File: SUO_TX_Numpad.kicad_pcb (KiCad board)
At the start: 2 copper layers, 79.1 x 127.6 mm, 93 parts, among them J1 USB_C_Receptacle_USB2.0_16P, SW1 BOOT, U1 STM32F411CEUx, U2 XC6206PxxxMR-Regulator_Linear, U3 USBLC6-2SC6

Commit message: Added LCSC, but going to switch to 0603 or 0804 components as I want to keep handsoldering an option
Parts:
- F1: value Fuse 1500mA Fast -> Fuse 1A Fast

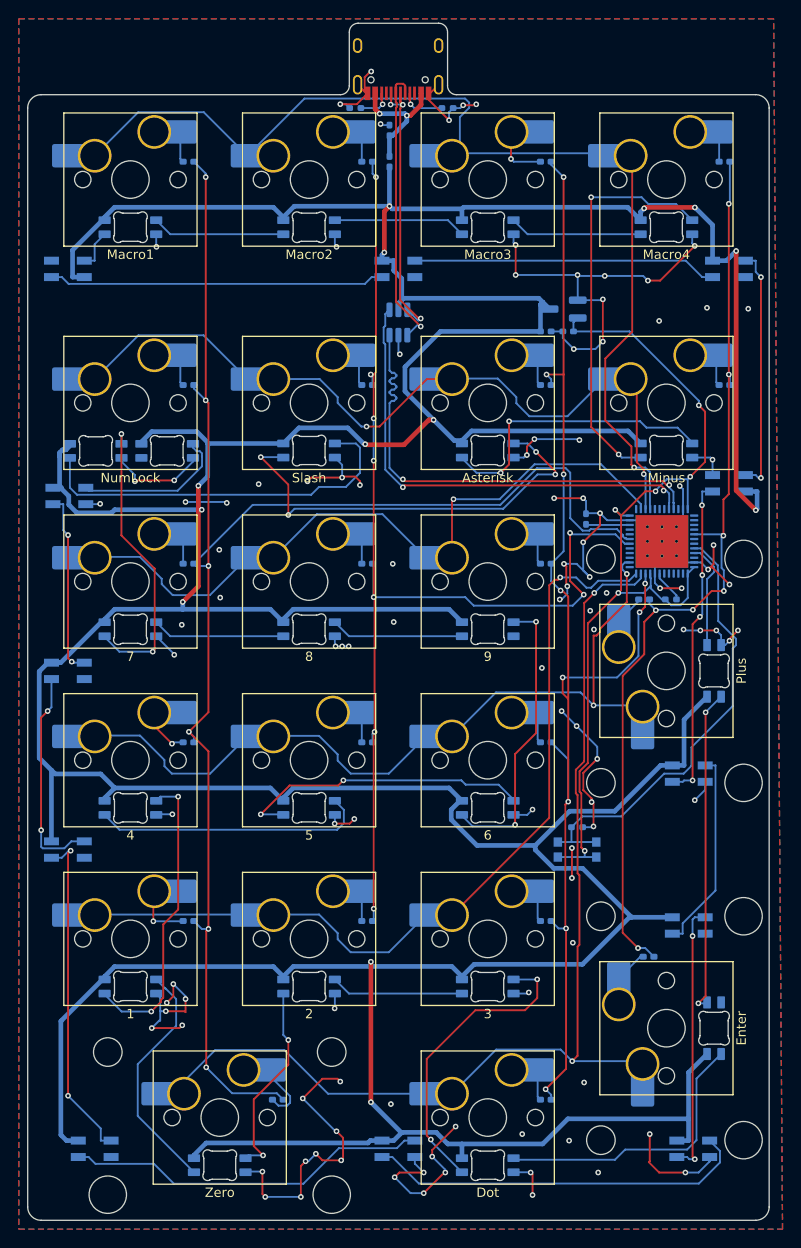
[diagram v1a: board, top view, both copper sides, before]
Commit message: Switched to 0805 for R C and SOD-123 for Diodes
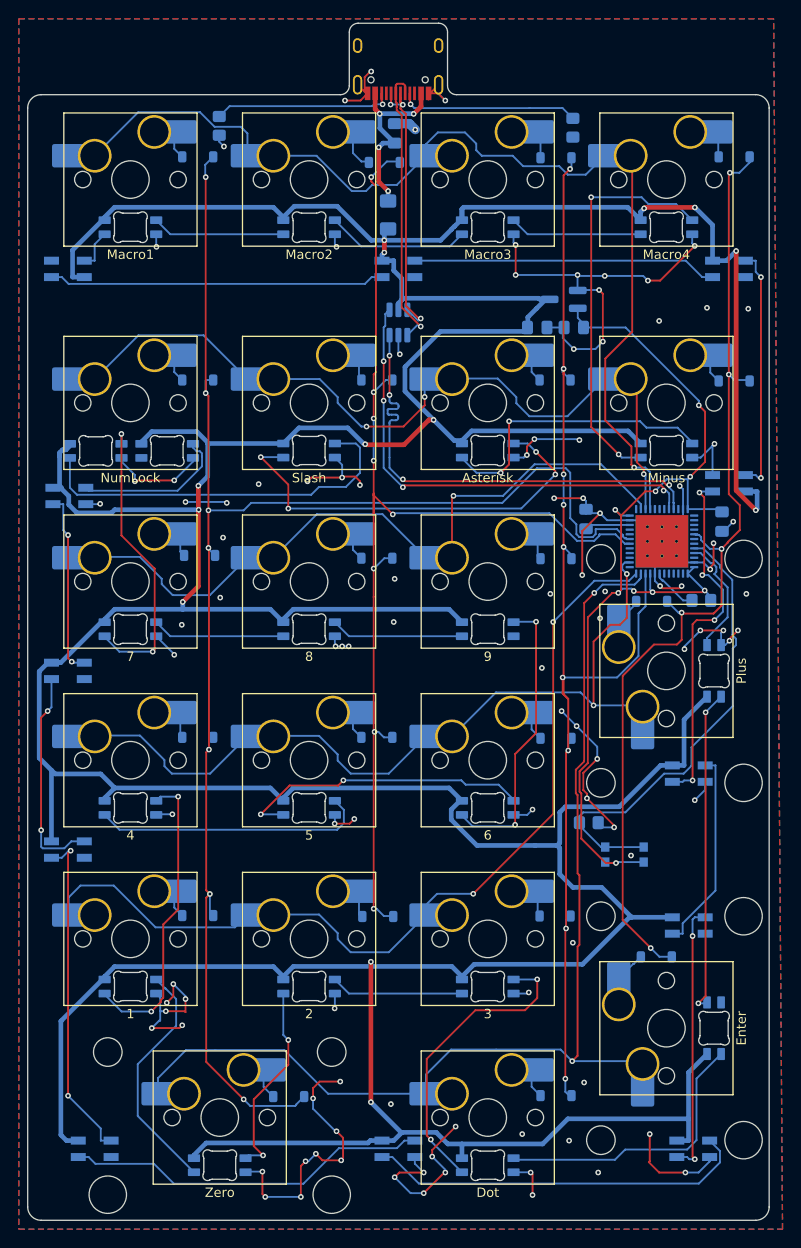
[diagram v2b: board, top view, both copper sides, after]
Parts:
- added C5: 10uF, Capacitor_SMD:C_0805_2012Metric_Pad1.18x1.45mm_HandSolder, B.Cu at (172.6, 79.3)
- C1, C2, C3, C4: footprint Capacitor_SMD:C_0402_1005Metric_Pad0.74x0.62mm_HandSolder -> Capacitor_SMD:C_0805_2012Metric_Pad1.18x1.45mm_HandSolder
- D1, D10, D11, D12, D13, D14, D15, D16, D17, D18, D19, D2, D20, D21, D3, D4, D5, D6, D7, D8, D9: footprint Diode_SMD:D_0402_1005Metric_Pad0.77x0.64mm_HandSolder -> ScottoKeebs_Components:Diode_SOD-123
- F1: value Fuse 1A Fast -> 1.5A; footprint Fuse:Fuse_0402_1005Metric_Pad0.77x0.64mm_HandSolder -> Fuse:Fuse_1206_3216Metric_Pad1.42x1.75mm_HandSolder
- R1, R2, R3, R4: footprint Resistor_SMD:R_0402_1005Metric_Pad0.72x0.64mm_HandSolder -> Resistor_SMD:R_0805_2012Metric_Pad1.20x1.40mm_HandSolder
- moved R2 14.6 mm to (119.0, 37.1), turned to -90 degrees
- moved R1 13.5 mm to (156.7, 37.3), turned to -90 degrees
- moved F1 5.68 mm to (137.0, 46.6)
- moved SW1 5.08 mm to (162.2, 114.8)
- moved R4 3.25 mm to (170.4, 87.7), turned to 0 degrees
- moved D2 1.84 mm to (136.6, 41.0)
- moved D9 1.48 mm to (116.9, 82.9)
- moved R3 1.34 mm to (158.4, 111.4)
- moved D17 1.23 mm to (135.9, 121.4)
- moved D11 1.21 mm to (154.9, 83.3)
- moved D20 1.21 mm to (126.4, 140.6)
- moved D10 1.19 mm to (135.8, 83.2)
- moved D15 1.17 mm to (154.9, 102.4)
- moved D21 1.17 mm to (154.9, 140.5)
- moved D14 1.16 mm to (135.8, 102.3)
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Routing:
- net Net-(J1-CC2): track 4.23 -> 19.7 mm
- net Net-(J1-CC1): track 5.74 -> 20.2 mm
- net +3V3: track 98.6 -> 107.9 mm, vias 6 -> 9
- net GND: track 289.0 -> 280.0 mm, vias 111 -> 106
- net ROW6: track 119.0 -> 127.3 mm
- net COL3: track 136.1 -> 128.6 mm, vias 10 -> 9
- net COL4: track 100.4 -> 107.5 mm, vias 7 -> 5
- net USB_5V: track 14.6 -> 21.6 mm, vias 2 -> 4
- net ROW5: track 94.8 -> 99.5 mm, vias 1 -> 2
- net ROW1: track 121.5 -> 117.5 mm
- net Net-(UNDER4-DOUT): track 34.6 -> 38.4 mm
- net VBUS: track 625.9 -> 622.3 mm
- net Net-(D20-A): track 10.5 -> 7.08 mm
- net Net-(D16-A): track 9.21 -> 6.13 mm, vias 1 -> 0
- net Net-(U1-NRST): track 3.50 -> 5.54 mm
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
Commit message: Updated BOM
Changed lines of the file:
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@@
 		)
 		(pad "A1" smd rect
-			(at -3.25 -4.045 180)
-			(size 0.6 1.45)
+			(at -3.255 -4.045 180)
+			(size 0.59 1.45)
 			(layers "F.Cu" "F.Mask" "F.Paste")
 			(net 14 "GND")
@@
 		(pad "A4" smd rect
 			(at -2.45 -4.045 180)
-			(size 0.6 1.45)
+			(size 0.58 1.45)
 			(layers "F.Cu" "F.Mask" "F.Paste")
 			(net 19 "USB_5V")
@@
 		(pad "A5" smd rect
 			(at -1.25 -4.045 180)
-			(size 0.3 1.45)
+			(size 0.28 1.45)
 			(layers "F.Cu" "F.Mask" "F.Paste")
 			(net 20 "Net-(J1-CC1)")
@@
 		(pad "A6" smd rect
 			(at -0.25 -4.045 180)
-			(size 0.3 1.45)
+			(size 0.28 1.45)
 			(layers "F.Cu" "F.Mask" "F.Paste")
 			(net 21 "USB_D+")
@@
 		(pad "A7" smd rect
 			(at 0.25 -4.045 180)
-			(size 0.3 1.45)
+			(size 0.28 1.45)
 			(layers "F.Cu" "F.Mask" "F.Paste")
 			(net 22 "USB_D-")
@@
 		(pad "A8" smd rect
 			(at 1.25 -4.045 180)
-			(size 0.3 1.45)
+			(size 0.28 1.45)
 			(layers "F.Cu" "F.Mask" "F.Paste")
 			(net 23 "unconnected-(J1-SBU1-PadA8)")
@@
 		(pad "A9" smd rect
 			(at 2.45 -4.045 180)
-			(size 0.6 1.45)
+			(size 0.58 1.45)
 			(layers "F.Cu" "F.Mask" "F.Paste")
 			(net 19 "USB_5V")
@@
 		)
 		(pad "A12" smd rect
-			(at 3.25 -4.045 180)
-			(size 0.6 1.45)
+			(at 3.255 -4.045 180)
+			(size 0.59 1.45)
 			(layers "F.Cu" "F.Mask" "F.Paste")
 			(net 14 "GND")
@@
 		)
 		(pad "B1" smd rect
-			(at 3.25 -4.045 180)
-			(size 0.6 1.45)
+			(at 3.255 -4.045 180)
+			(size 0.59 1.45)
 			(layers "F.Cu" "F.Mask" "F.Paste")
 			(net 14 "GND")
@@
 		(pad "B4" smd rect
 			(at 2.45 -4.045 180)
-			(size 0.6 1.45)
+			(size 0.58 1.45)
 			(layers "F.Cu" "F.Mask" "F.Paste")
 			(net 19 "USB_5V")
@@
 		(pad "B5" smd rect
 			(at 1.75 -4.045 180)
-			(size 0.3 1.45)
+			(size 0.28 1.45)
 			(layers "F.Cu" "F.Mask" "F.Paste")
 			(net 24 "Net-(J1-CC2)")
@@
 		(pad "B6" smd rect
 			(at 0.75 -4.045 180)
-			(size 0.3 1.45)
+			(size 0.28 1.45)
 			(layers "F.Cu" "F.Mask" "F.Paste")
 			(net 21 "USB_D+")
@@
 		(pad "B7" smd rect
 			(at -0.75 -4.045 180)
-			(size 0.3 1.45)
+			(size 0.28 1.45)
 			(layers "F.Cu" "F.Mask" "F.Paste")
 			(net 22 "USB_D-")
@@
 		(pad "B8" smd rect
 			(at -1.75 -4.045 180)
-			(size 0.3 1.45)
+			(size 0.28 1.45)
 			(layers "F.Cu" "F.Mask" "F.Paste")
 			(net 25 "unconnected-(J1-SBU2-PadB8)")
@@
 		(pad "B9" smd rect
 			(at -2.45 -4.045 180)
-			(size 0.6 1.45)
+			(size 0.58 1.45)
 			(layers "F.Cu" "F.Mask" "F.Paste")
 			(net 19 "USB_5V")
@@
 		)
 		(pad "B12" smd rect
-			(at -3.25 -4.045 180)
-			(size 0.6 1.45)
+			(at -3.255 -4.045 180)
+			(size 0.59 1.45)
 			(layers "F.Cu" "F.Mask" "F.Paste")
 			(net 14 "GND")
@@
 			)
 		)
-		(property "LCSC" "C60490"
+		(property "LCSC" "C2930231"
 			(at 0 0 0)
 			(unlocked yes)
@@
 			)
 		)
-		(property "LCSC" "C32949"
+		(property "LCSC" "C5137467"
 			(at 0 0 90)
 			(unlocked yes)
@@
 			)
 		)
-		(property "LCSC" "C315248"
+		(property "LCSC" "C49010152"
 			(at 0 0 0)
 			(unlocked yes)
@@
 			)
 		)
-		(property "LCSC" "C315248"
+		(property "LCSC" "C49010152"
 			(at 0 0 90)
 			(unlocked yes)
@@
 			)
 		)
-		(property "LCSC" "C105872"
+		(property "LCSC" "C2930296"
 			(at 0 0 270)
 			(unlocked yes)
@@
 			)
 		)
-		(property "LCSC" "C315248"
+		(property "LCSC" "C49010152"
 			(at 0 0 180)
 			(unlocked yes)
@@
 		(pad "49" smd rect
 			(at 0 0 90)
-			(size 5.6 5.6)
+			(size 5.56 5.56)
 			(property pad_prop_heatsink)
 			(layers "F.Cu")
@@
 		(pad "49" smd rect
 			(at 0 0 90)
-			(size 5.6 5.6)
+			(size 5.56 5.56)
 			(property pad_prop_heatsink)
 			(layers "B.Cu" "B.Mask")
@@
 			)
 		)
-		(property "LCSC" "C315248"
+		(property "LCSC" "C49010152"
 			(at 0 0 90)
 			(unlocked yes)
@@
 			)
 		)
-		(property "LCSC" "C60490"
+		(property "LCSC" "C2930231"
 			(at 0 0 180)
 			(unlocked yes)
@@
 			)
 		)
-		(property "LCSC" "C105872"
+		(property "LCSC" "C2930296"
 			(at 0 0 270)
 			(unlocked yes)

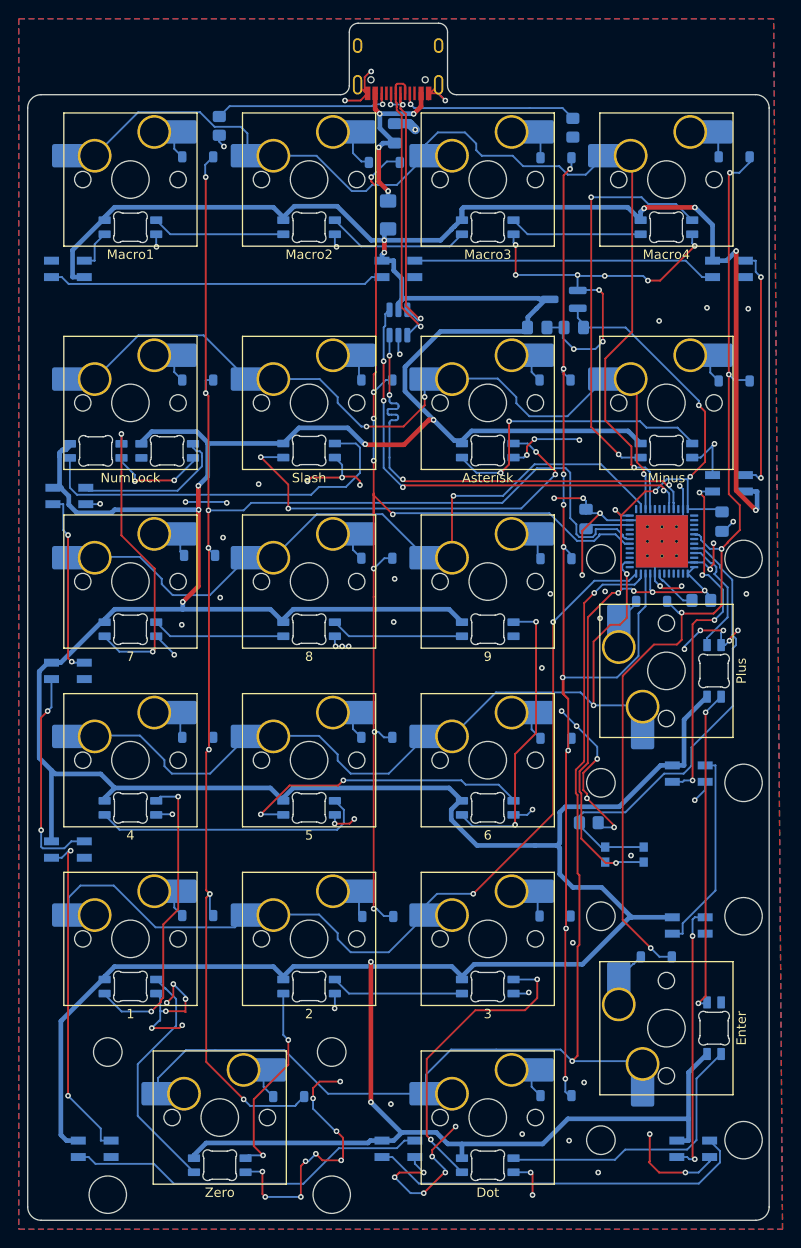
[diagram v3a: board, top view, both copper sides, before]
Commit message: PCB Layout altered to be exact to a SUO TX TKL board, Y-dimensions-wise
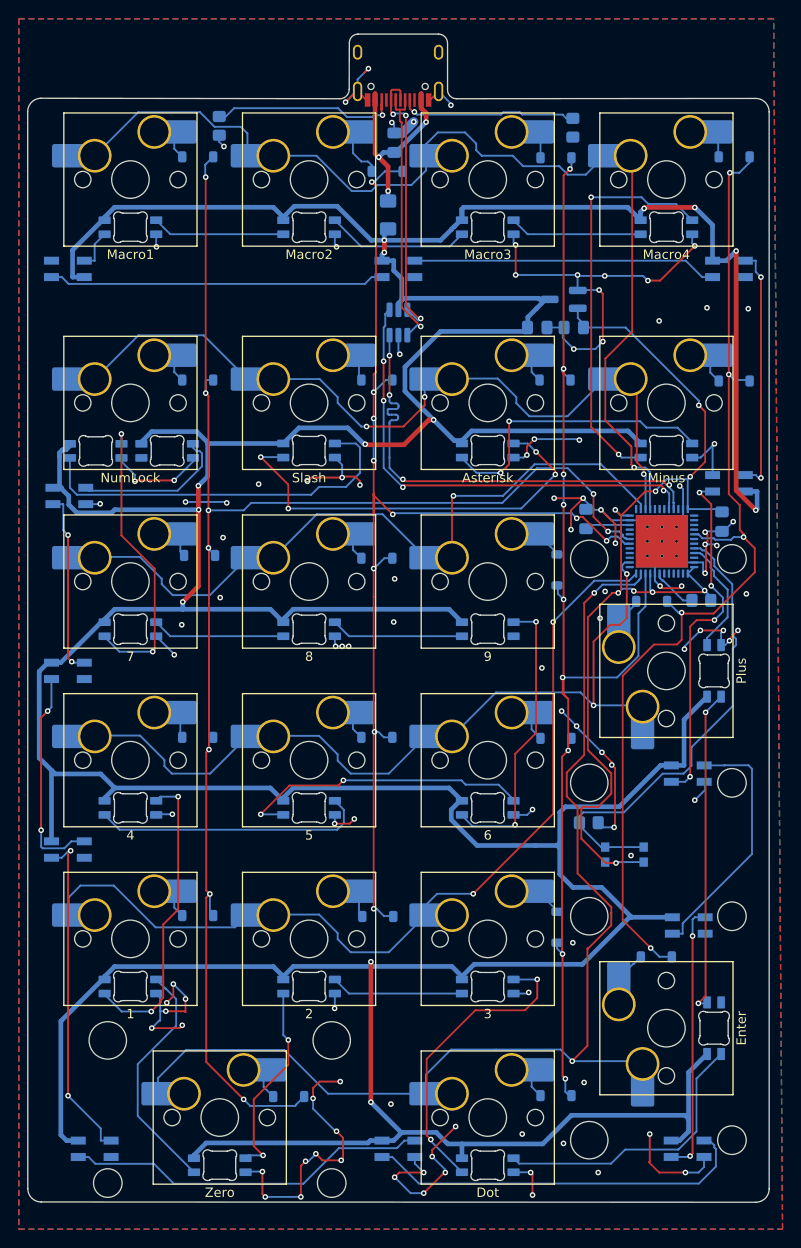
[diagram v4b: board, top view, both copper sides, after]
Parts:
- moved D18 1.21 mm to (155.0, 122.6), turned to 90 degrees
- moved D11 1.20 mm to (155.0, 84.5), turned to 90 degrees
- moved C1 1.00 mm to (137.7, 38.9)
- moved D2 0.99 mm to (136.9, 42.0)
- moved J1 0.71 mm to (138.1, 30.3)
- moved UNDER7 0.60 mm to (168.9, 146.2)
- moved UNDER5 0.11 mm to (169.0, 106.2)
- turned STAB1 to -90 degrees
- turned STAB2 to -90 degrees
- turned STAB3 to 180 degrees
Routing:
- net Net-(UNDER5-DOUT): track 21.6 -> 27.0 mm
- net ROW6: track 127.3 -> 130.9 mm
- net COL4: track 107.5 -> 111.0 mm
- net GND: track 280.0 -> 283.4 mm, vias 106 -> 109
- net COL1: track 172.1 -> 169.0 mm, vias 7 -> 9
- net +3V3: track 107.9 -> 110.7 mm
- net USB_5V: track 21.6 -> 22.7 mm, vias 4 -> 3
- net Net-(J1-CC1): track 20.2 -> 19.0 mm
- net Net-(D2-A): track 7.84 -> 8.91 mm
- net ROW1: track 117.5 -> 118.5 mm
- net Net-(UNDER4-DOUT): track 38.4 -> 37.6 mm
- net COL2: track 124.3 -> 123.6 mm, vias 8 -> 10
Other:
- board size 79.1 x 127.6 mm -> 79.1 x 124.6 mm

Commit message: Made board slightly smaller, un-rotated the plus and enter stabilisers, they are supposed to go inward and not outward
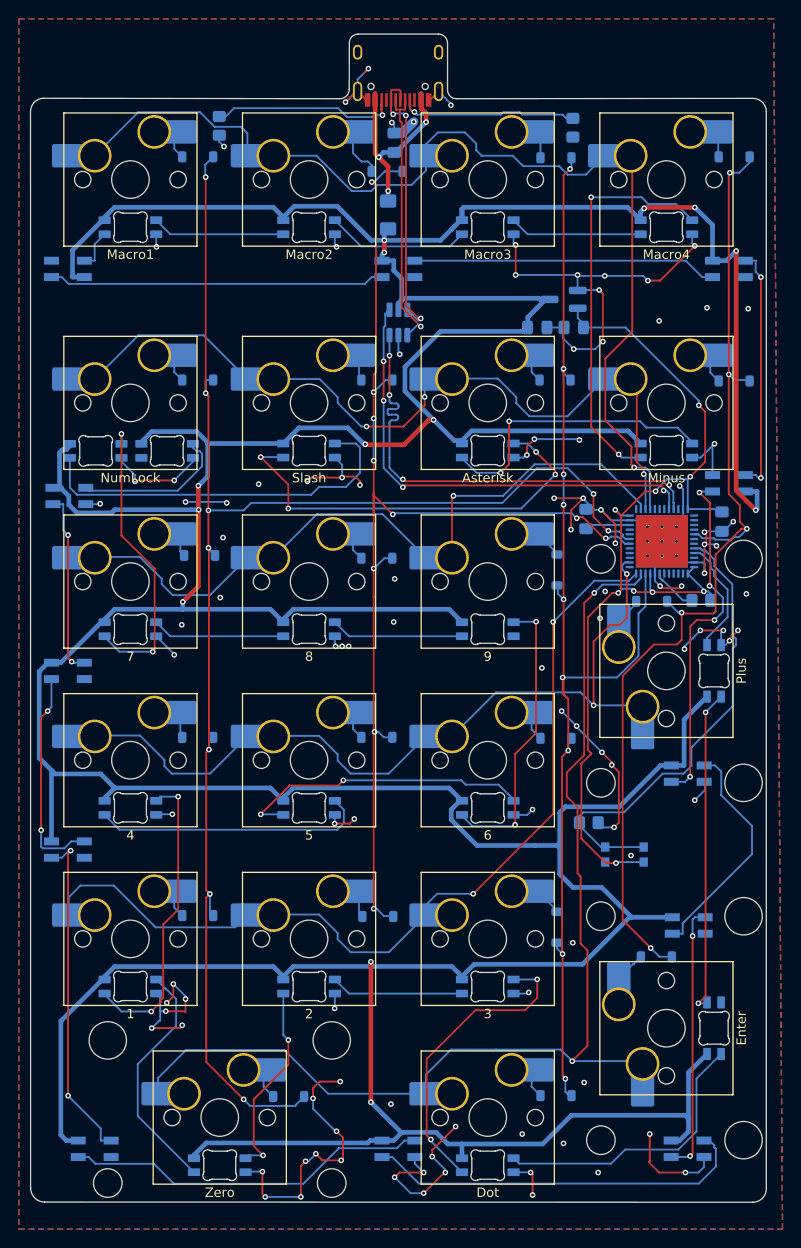
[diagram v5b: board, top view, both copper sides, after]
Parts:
- turned STAB1 to 90 degrees
- turned STAB2 to 90 degrees
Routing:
- net +3V3: track 110.7 -> 108.2 mm
- net ROW6: track 130.9 -> 128.8 mm
- net Net-(UNDER5-DOUT): track 27.0 -> 24.9 mm
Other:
- board size 79.1 x 124.6 mm -> 78.5 x 124.6 mm

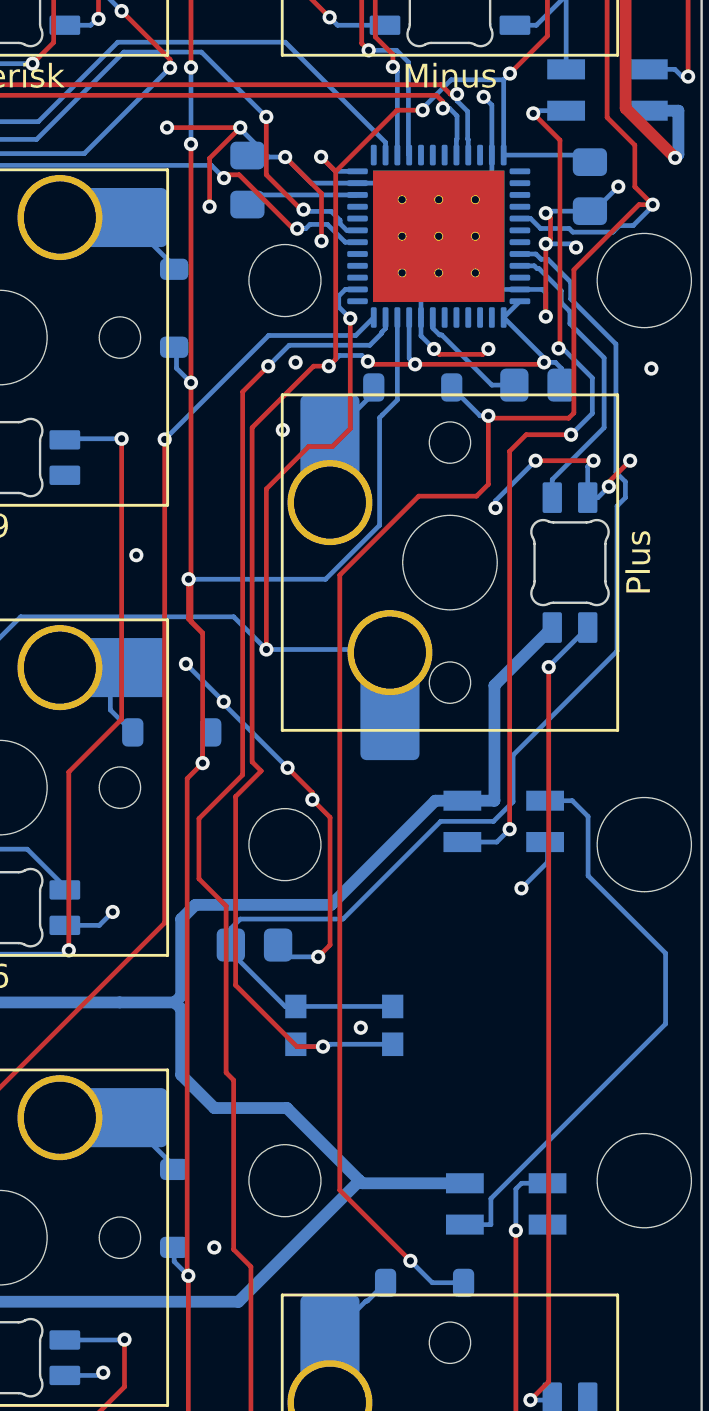
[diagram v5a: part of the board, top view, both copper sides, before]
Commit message: Fixed VCAP1 Value to 4.7 uF, added XTAL 8 MHz
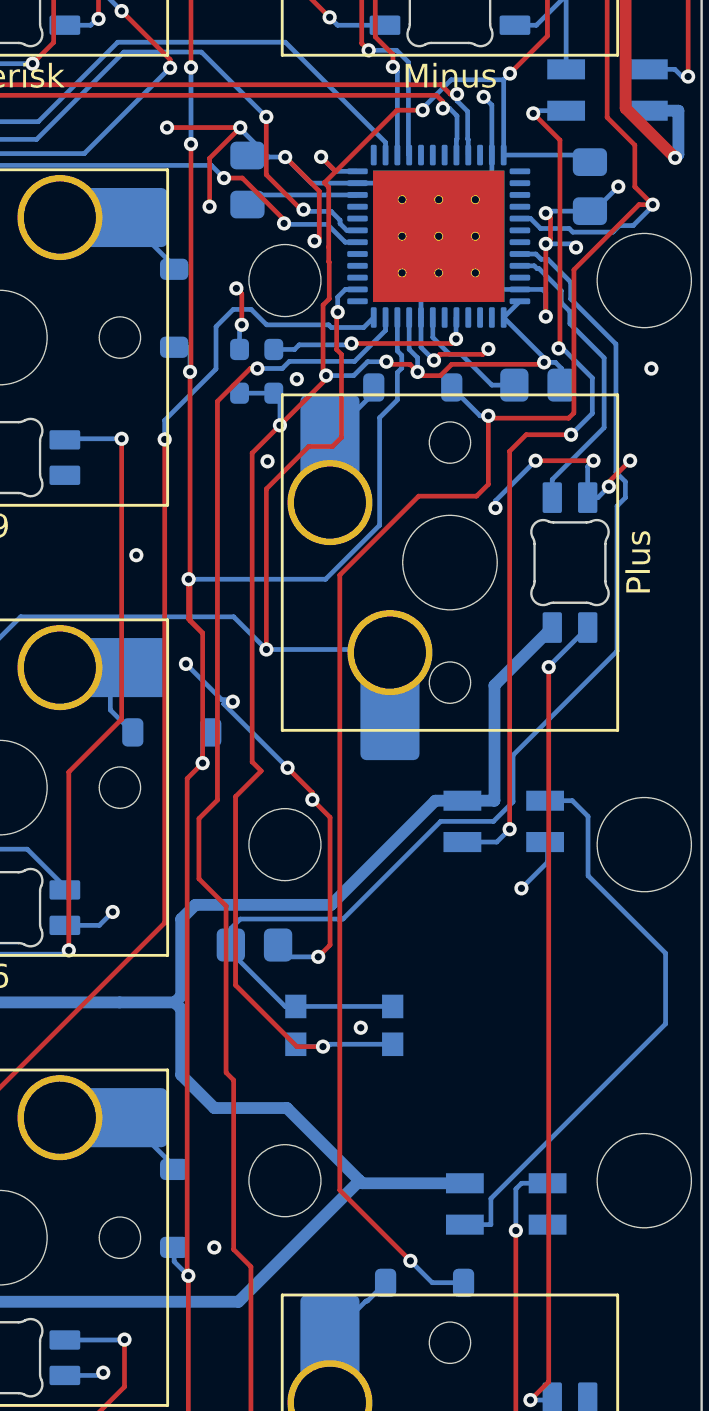
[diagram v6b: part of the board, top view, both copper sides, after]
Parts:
- added Y1: XTAL OSC XO 8.0000MHZ HCMOS SMD, Oscillator:Oscillator_SMD_ECS_2520MV-xxx-xx-4Pin_2.5x2.0mm, B.Cu at (158.5, 87.2)
- C4: value 10pF -> 4.7uF
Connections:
- U1 pad 5: unconnected-(U1-PH0-Pad5) -> Net-(U1-PH0)
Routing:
- net Net-(U1-PH0): track 0.00 -> 8.81 mm, vias 0 -> 2
- net GND: track 283.8 -> 287.8 mm, vias 109 -> 111
- net +3V3: track 108.2 -> 111.9 mm, vias 9 -> 10
- net ROW5: track 99.5 -> 101.7 mm
